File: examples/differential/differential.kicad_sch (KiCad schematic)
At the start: 4 parts

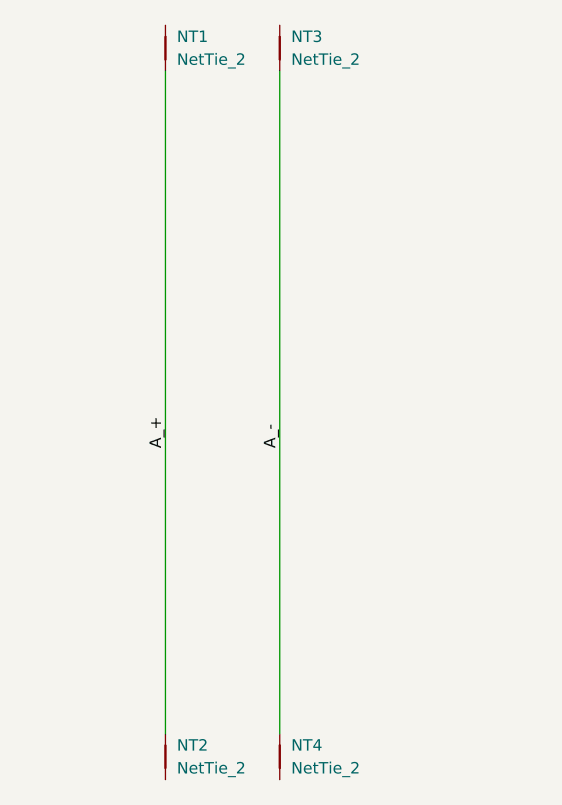
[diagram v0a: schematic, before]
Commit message: Update examples with corrected settings and keep track of exported gerbers
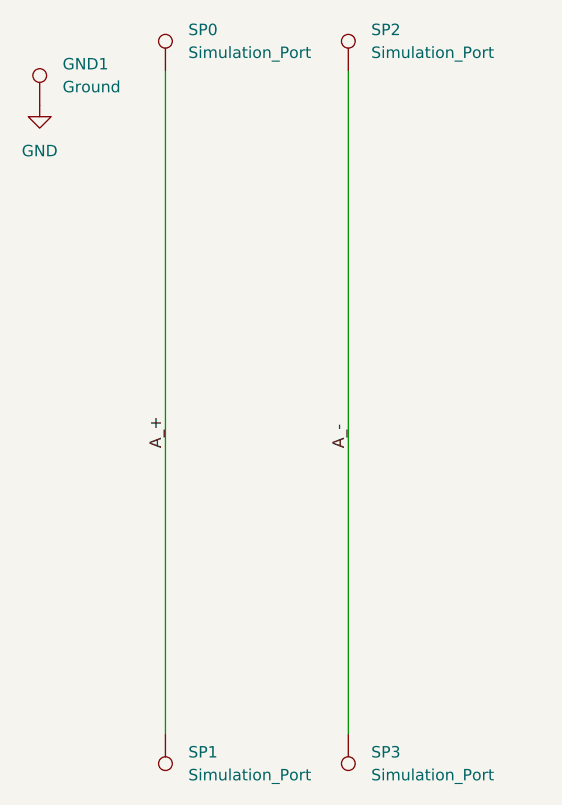
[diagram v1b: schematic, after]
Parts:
- removed NT1, NT2, NT3, NT4: NetTie_2, NetTie:NetTie-2_SMD_Pad0.5mm, symbol Device:NetTie_2
- added GND1: Ground, simulation_port:pad_0.15mm, symbol Connector:TestPoint
- added SP0, SP1, SP2, SP3: Simulation_Port, simulation_port:pad_0.5mm, symbol Connector:TestPoint
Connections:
- net A_+: now also SP0.1, SP1.1
- net A_-: now also SP2.1, SP3.1
- new net GND: GND1.1
